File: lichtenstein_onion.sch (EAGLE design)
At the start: 45 parts, among them IC1 LM2852Y-3V3, J1 MAGJACK, U1 ONION-OMEGA2

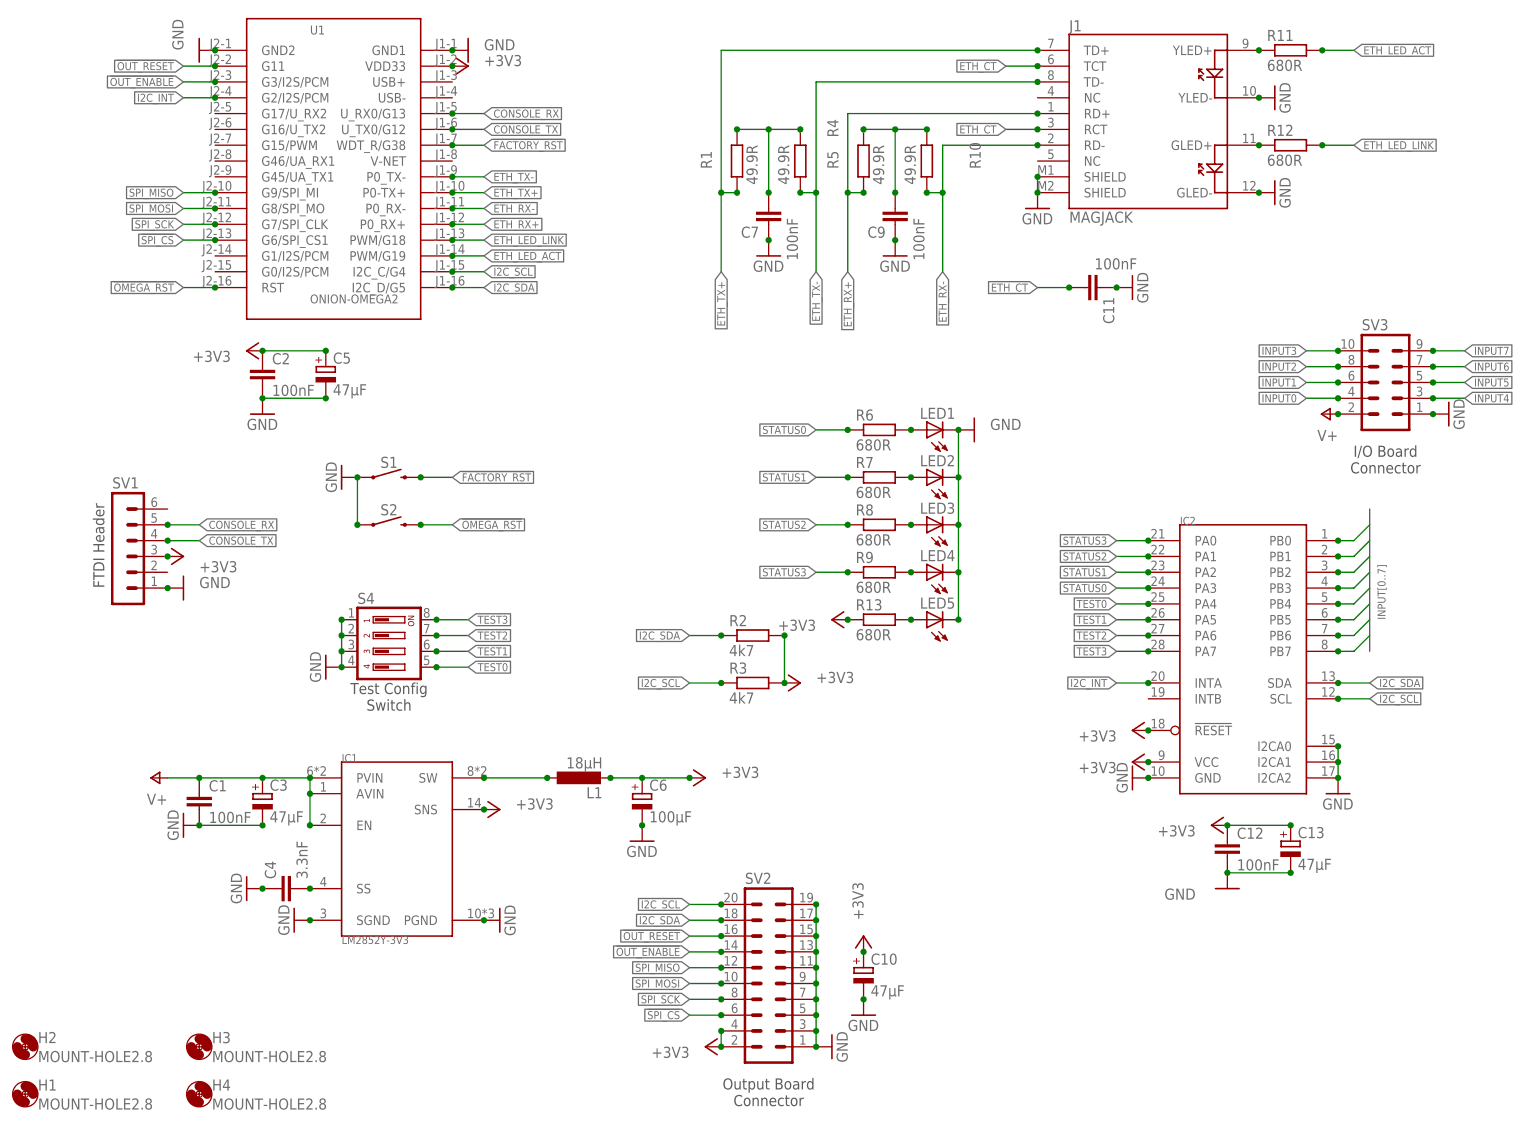
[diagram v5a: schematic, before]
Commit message: Fixed a few footprint issues and added explcit pull-ups for test inputs
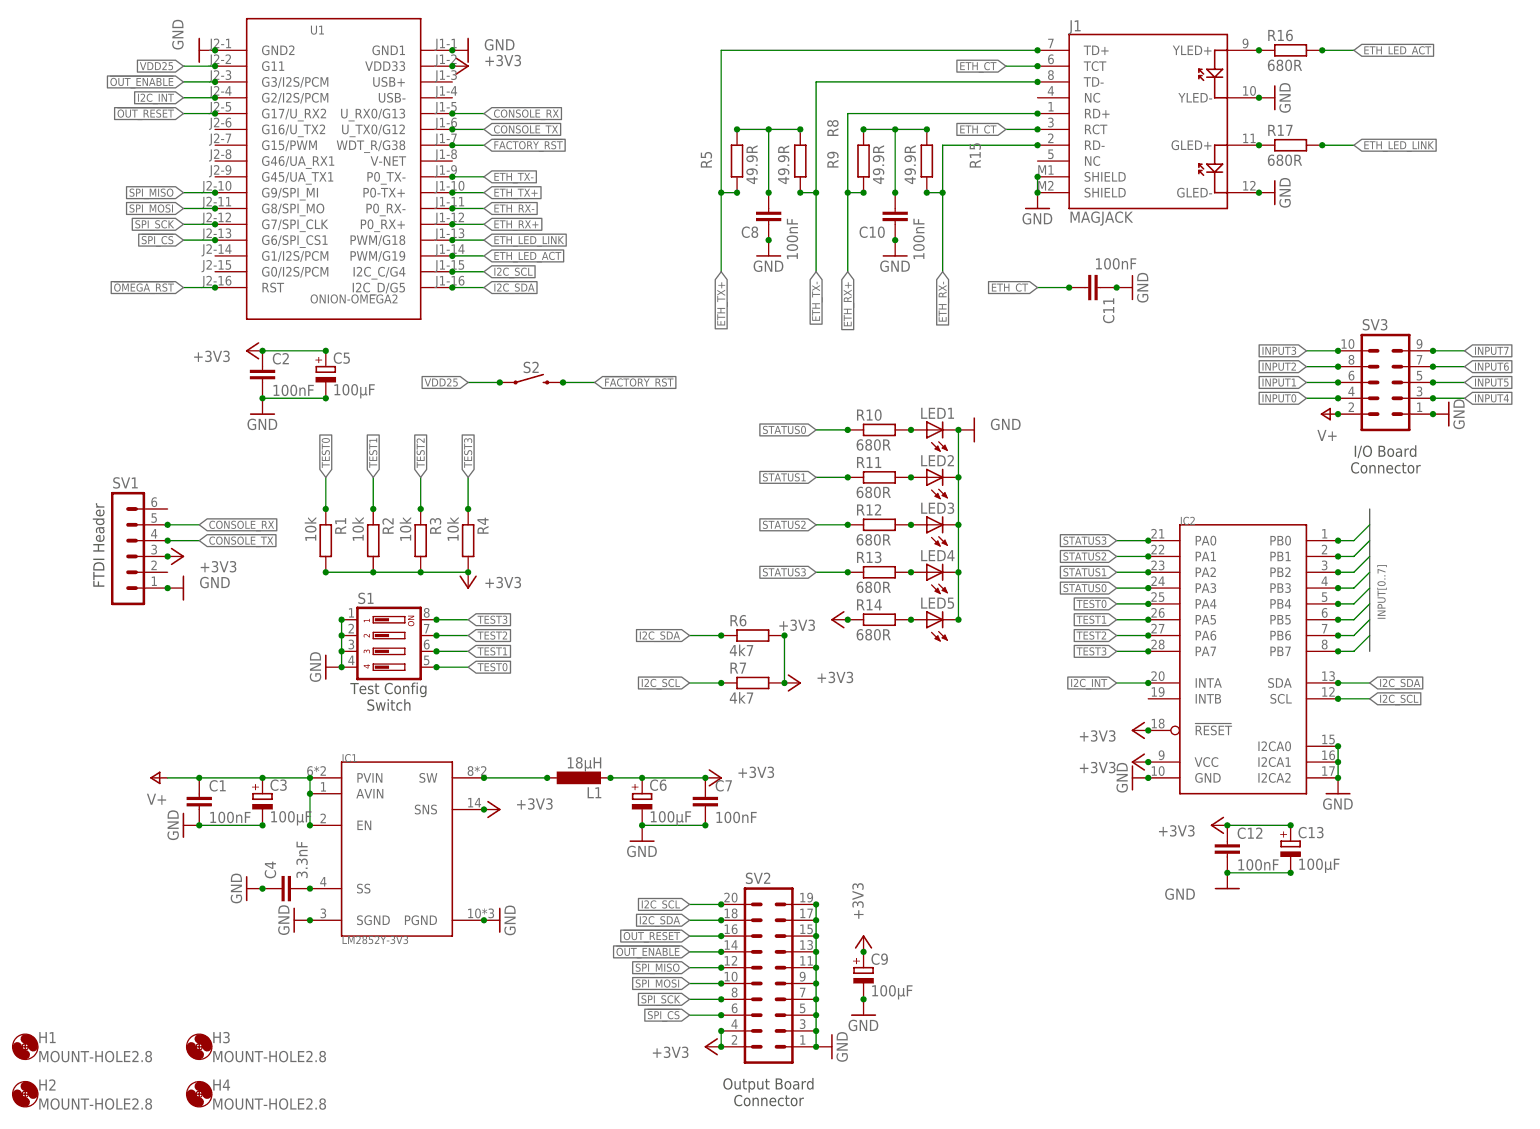
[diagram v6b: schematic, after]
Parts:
- removed S4: 219-04, switch-dil:219-04
- added C8: 100nF, rcl:C-EUC0805
- added R14, R16, R17: 680R, rcl:R-EU_M0805
- added R15: 49.9R, rcl:R-EU_M0805
- C10: value 47µF -> 100nF; device rcl:CPOL-EUCT6032 -> rcl:C-EUC0805; MOUSER 581-NOSD107M006 -> 710-885012207072
- C13, C3, C5: value 47µF -> 100µF; device rcl:CPOL-EUCT6032 -> rcl:CPOL-EUSMCD
- C9: value 100nF -> 100µF; device rcl:C-EUC0805 -> rcl:CPOL-EUSMCD; MOUSER 710-885012207072 -> 581-NOSD107M006
- R1, R4: value 49.9R -> 10k; MOUSER 652-CR0805-FX4701GLF -> 652-CR0805FX-1002ELF
- R10: value 49.9R -> 680R; MOUSER 652-CR0805-FX4701GLF -> 652-CR0805-FX6800GLF
- R2, R3: value 4k7 -> 10k; MOUSER 652-CR0805-FX4701GLF -> 652-CR0805FX-1002ELF
- R5: MOUSER 652-CR0805-FX4701GLF -> 652-CR0805FX-49R9ELF
- R6, R7: value 680R -> 4k7; MOUSER 652-CR0805-FX6800GLF -> 652-CR0805-FX4701GLF
- R8: value 680R -> 49.9R; MOUSER 652-CR0805-FX6800GLF -> 652-CR0805-FX4701GLF
- R9: value 680R -> 49.9R; MOUSER 652-CR0805-FX6800GLF -> 652-CR0805FX-49R9ELF
- S1: value MOMENTARY-SWITCH-SPST-PTH-6.0MM -> 219-04; device SparkFun-Switches:MOMENTARY-SWITCH-SPST-PTH-6.0MM -> switch-dil:219-04; MOUSER 612-TL1105B -> 774-219-4LPS
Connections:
- new net VDD25: S2.1, U1.G11
- net !FACTORY_RST: now also S2.2; no longer S1.2
- net !OMEGA_RST: no longer S2.2
- net !OUT_RESET: now also U1.G17/U_RX2; no longer U1.G11
- net +3V3: now also C7.1, C9.+, R1.2, R14.1, R4.2, R6.2, R7.2; no longer C10.+, R13.1
- net ETH_LED_ACT: now also R16.2; no longer R11.2
- net ETH_LED_LINK: now also R17.2; no longer R12.2
- net ETH_RX+: now also R9.1; no longer R5.1
- net ETH_RX-: now also R15.1; no longer R10.1
- net ETH_TX+: now also R5.1; no longer R1.1
- net ETH_TX-: now also R8.1; no longer R4.1
- net GND: now also C10.1, C7.2, C8.1, C9.-, S1.2, S1.3, S1.4; no longer C10.-, C7.1, C9.1, S2.1, S4.1, S4.2, S4.3, S4.4
- net I2C_SCL: now also R7.1; no longer R3.1
- net I2C_SDA: now also R6.1; no longer R2.1
- net N$1: now also R14.2; no longer R13.2
- net N$10: now also R12.2; no longer R8.2
- net N$11: now also R13.2; no longer R9.2
- net N$2: now also R10.2; no longer R6.2
- net N$3: now also C8.2, R5.2, R8.2; no longer C7.2, R1.2, R4.2
- net N$4: now also R16.1; no longer R11.1
- net N$5: now also R17.1; no longer R12.1
- net N$6: now also C10.2, R15.2, R9.2; no longer C9.2, R10.2, R5.2
- net N$9: now also R11.2; no longer R7.2
- net STATUS0: now also R10.1; no longer R6.1
- net STATUS1: now also R11.1; no longer R7.1
- net STATUS2: now also R12.1; no longer R8.1
- net STATUS3: now also R13.1; no longer R9.1
- net TEST0: now also R1.1, S1.5; no longer S4.5
- net TEST1: now also R2.1, S1.6; no longer S4.6
- net TEST2: now also R3.1, S1.7; no longer S4.7
- net TEST3: now also R4.1, S1.8; no longer S4.8
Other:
- moved on the sheet: C7, H1, H2, R1, R10, R11, R12, R13, R2, R3, R4, R5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

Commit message: Fixed bulk capacitor footprints; made +V for output channels independent on output board
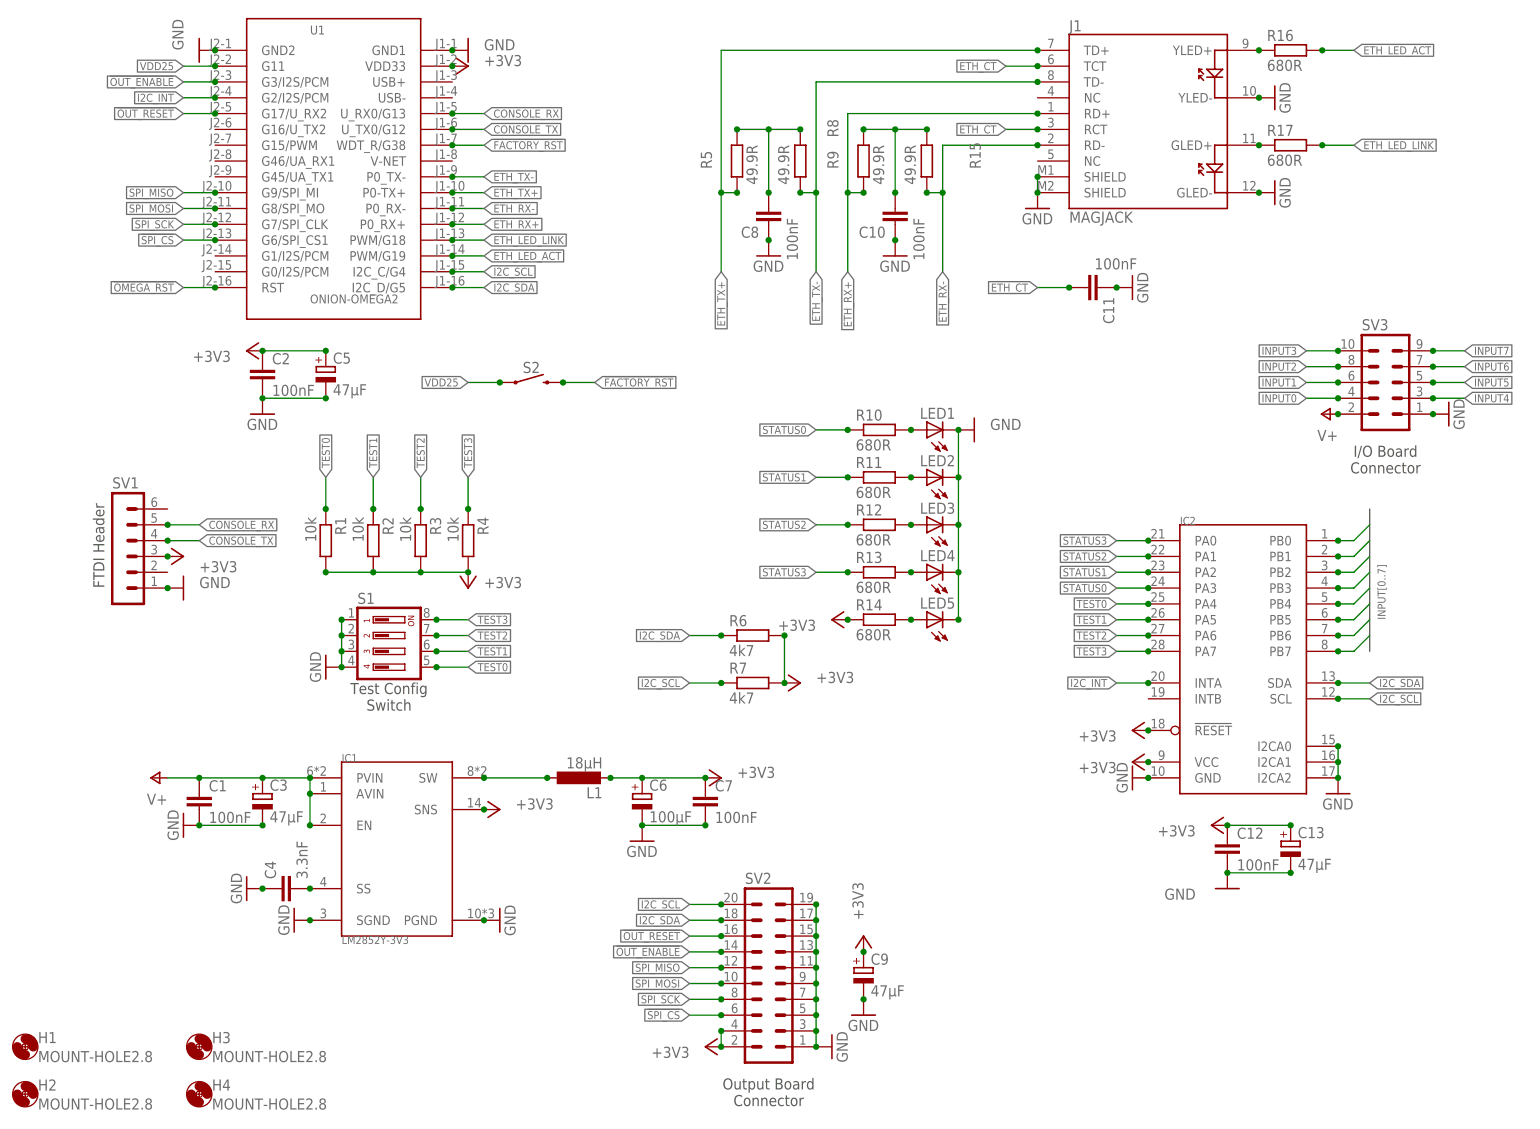
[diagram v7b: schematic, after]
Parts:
- C13, C3, C5: value 100µF -> 47µF; device rcl:CPOL-EUSMCD -> rcl:CPOL-EUCT7343; MOUSER 581-NOSD107M006 -> 581-TAJD476M016RNJV
- C6: device rcl:CPOL-EUSMCD -> rcl:CPOL-EUCT7343
- C9: value 100µF -> 47µF; MOUSER 581-NOSD107M006 -> 581-TAJD476M016RNJV
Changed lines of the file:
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@@
 <?xml version="1.0" encoding="utf-8"?>
 <!DOCTYPE eagle SYSTEM "eagle.dtd">
-<eagle version="8.7.0">
+<eagle version="9.0.1">
 <drawing>
 <settings>
@@
 <part name="L1" library="lichtenstein_onion" deviceset="SRR1050A" device="" value="18µH"/>
 <part name="+3V37" library="supply1" library_urn="urn:adsk.eagle:library:371" deviceset="+3V3" device=""/>
-<part name="C6" library="rcl" library_urn="urn:adsk.eagle:library:334" deviceset="CPOL-EU" device="SMCD" package3d_urn="urn:adsk.eagle:package:23434/1" value="100µF">
+<part name="C6" library="rcl" library_urn="urn:adsk.eagle:library:334" deviceset="CPOL-EU" device="CT7343" package3d_urn="urn:adsk.eagle:package:23304/2" value="100µF">
 <spice>
 <pinmapping spiceprefix="C">
@@
 <part name="GND10" library="supply1" library_urn="urn:adsk.eagle:library:371" deviceset="GND" device=""/>
 <part name="+3V35" library="supply1" library_urn="urn:adsk.eagle:library:371" deviceset="+3V3" device=""/>
-<part name="C3" library="rcl" library_urn="urn:adsk.eagle:library:334" deviceset="CPOL-EU" device="SMCD" package3d_urn="urn:adsk.eagle:package:23434/1" value="100µF">
+<part name="C3" library="rcl" library_urn="urn:adsk.eagle:library:334" deviceset="CPOL-EU" device="CT7343" package3d_urn="urn:adsk.eagle:package:23304/2" value="47µF">
 <spice>
 <pinmapping spiceprefix="C">
@@
 </pinmapping>
 </spice>
-<attribute name="MOUSER" value="581-NOSD107M006"/>
+<attribute name="MOUSER" value="581-TAJD476M016RNJV"/>
 </part>
 <part name="C1" library="rcl" library_urn="urn:adsk.eagle:library:334" deviceset="C-EU" device="C0805" package3d_urn="urn:adsk.eagle:package:23617/2" value="100nF">
@@
 </part>
 <part name="GND2" library="supply1" library_urn="urn:adsk.eagle:library:371" deviceset="GND" device=""/>
-<part name="C5" library="rcl" library_urn="urn:adsk.eagle:library:334" deviceset="CPOL-EU" device="SMCD" package3d_urn="urn:adsk.eagle:package:23434/1" value="100µF">
+<part name="C5" library="rcl" library_urn="urn:adsk.eagle:library:334" deviceset="CPOL-EU" device="CT7343" package3d_urn="urn:adsk.eagle:package:23304/2" value="47µF">
 <spice>
 <pinmapping spiceprefix="C">
@@
 </pinmapping>
 </spice>
-<attribute name="MOUSER" value="581-NOSD107M006"/>
+<attribute name="MOUSER" value="581-TAJD476M016RNJV"/>
 </part>
 <part name="SV1" library="con-lstb" library_urn="urn:adsk.eagle:library:162" deviceset="MA06-1" device="" package3d_urn="urn:adsk.eagle:package:8340/1"/>
@@
 <part name="GND19" library="supply1" library_urn="urn:adsk.eagle:library:371" deviceset="GND" device=""/>
 <part name="+3V313" library="supply1" library_urn="urn:adsk.eagle:library:371" deviceset="+3V3" device=""/>
-<part name="C13" library="rcl" library_urn="urn:adsk.eagle:library:334" deviceset="CPOL-EU" device="SMCD" package3d_urn="urn:adsk.eagle:package:23434/1" value="100µF">
+<part name="C13" library="rcl" library_urn="urn:adsk.eagle:library:334" deviceset="CPOL-EU" device="CT7343" package3d_urn="urn:adsk.eagle:package:23304/2" value="47µF">
 <spice>
 <pinmapping spiceprefix="C">
@@
 </pinmapping>
 </spice>
-<attribute name="MOUSER" value="581-NOSD107M006"/>
+<attribute name="MOUSER" value="581-TAJD476M016RNJV"/>
 </part>
 <part name="GND22" library="supply1" library_urn="urn:adsk.eagle:library:371" deviceset="GND" device=""/>
@@
 <part name="GND13" library="supply1" library_urn="urn:adsk.eagle:library:371" deviceset="GND" device=""/>
 <part name="+3V310" library="supply1" library_urn="urn:adsk.eagle:library:371" deviceset="+3V3" device=""/>
-<part name="C9" library="rcl" library_urn="urn:adsk.eagle:library:334" deviceset="CPOL-EU" device="SMCD" package3d_urn="urn:adsk.eagle:package:23434/1" value="100µF">
+<part name="C9" library="rcl" library_urn="urn:adsk.eagle:library:334" deviceset="CPOL-EU" device="SMCD" package3d_urn="urn:adsk.eagle:package:23434/1" value="47µF">
 <spice>
 <pinmapping spiceprefix="C">
@@
 </pinmapping>
 </spice>
-<attribute name="MOUSER" value="581-NOSD107M006"/>
+<attribute name="MOUSER" value="581-TAJD476M016RNJV"/>
 </part>
 <part name="+3V36" library="supply1" library_urn="urn:adsk.eagle:library:371" deviceset="+3V3" device=""/>
